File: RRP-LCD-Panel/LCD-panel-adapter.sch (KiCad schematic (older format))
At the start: 4 parts, among them J101 HEADER_18, P101 CONN_4X2, P102 CONN_5X2, P103 CONN_5X2

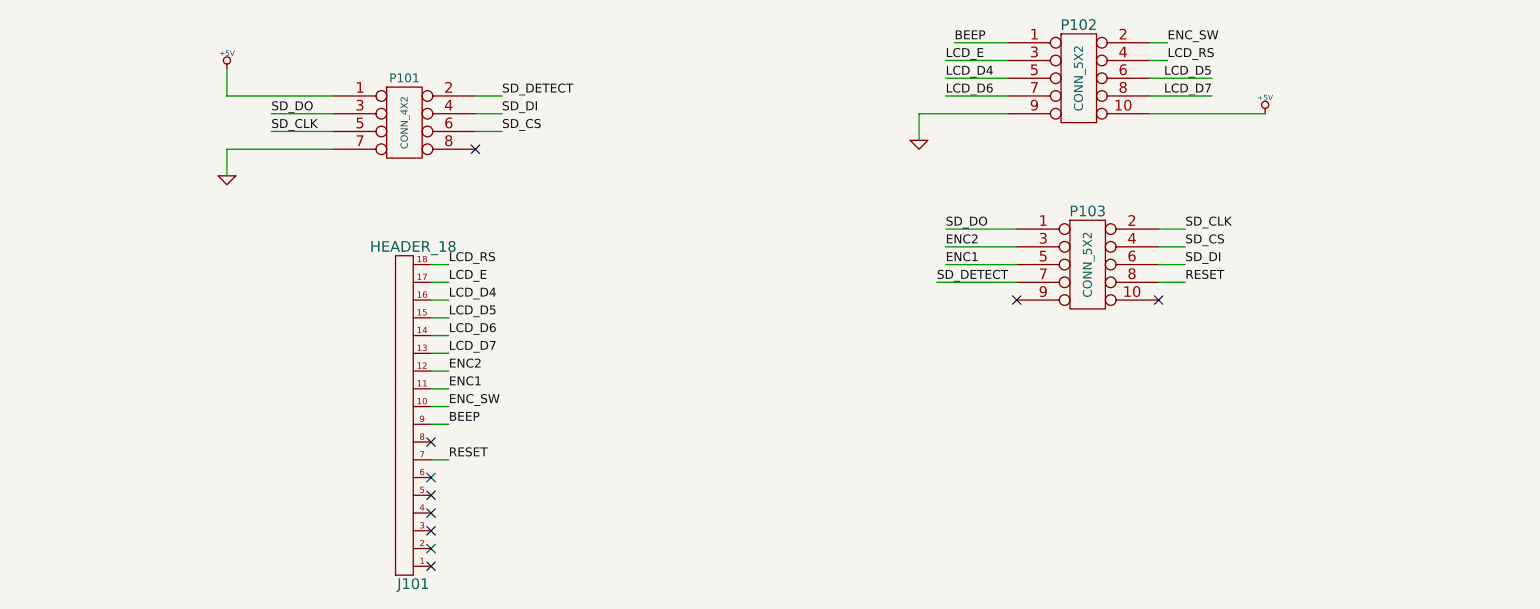
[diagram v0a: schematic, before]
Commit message: RRP-LCD-Panel: update schematics, add PDFS
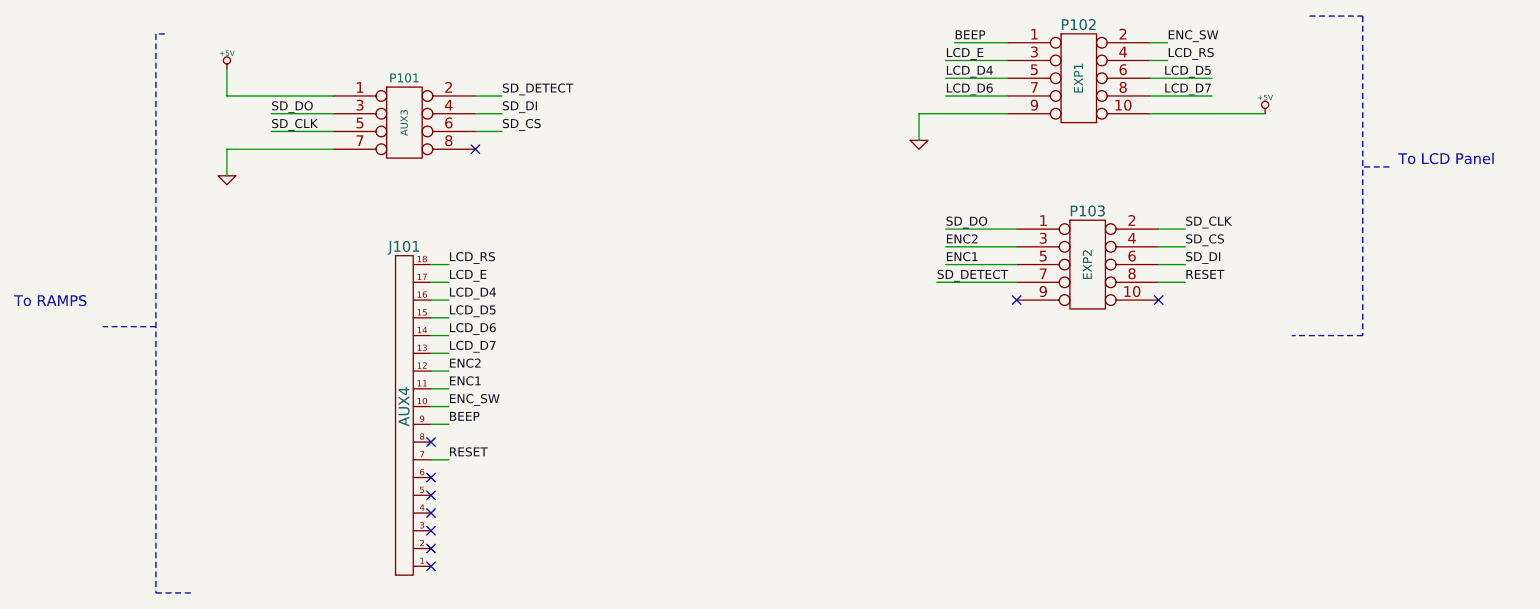
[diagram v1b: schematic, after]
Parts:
- J101: value HEADER_18 -> AUX4
- P101: value CONN_4X2 -> AUX3
- P102: value CONN_5X2 -> EXP1
- P103: value CONN_5X2 -> EXP2
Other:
- note added: "To LCD Panel"
- note added: "To RAMPS"
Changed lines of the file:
@@
 encoding utf-8
 Sheet 1 1
-Title ""
-Date "25 sep 2013"
+Title "RepRap LCD Controller - RAMPS Adapter"
+Date "3 oct 2013"
 Rev ""
-Comp ""
-Comment1 ""
-Comment2 ""
+Comp "Based on http://reprap.org/wiki/RepRapDiscount_Smart_Controller"
+Comment1 "License: GPL"
+Comment2 "Drawn by: Bob Cousins"
 Comment3 ""
 Comment4 ""
@@
 P 6750 1950
 F 0 "P102" H 6750 2250 60  0000 C CNN
-F 1 "CONN_5X2" V 6750 1950 50  0000 C CNN
+F 1 "EXP1" V 6750 1950 50  0000 C CNN
 F 2 "" H 6750 1950 60  0000 C CNN
 F 3 "" H 6750 1950 60  0000 C CNN
@@
 P 6800 3000
 F 0 "P103" H 6800 3300 60  0000 C CNN
-F 1 "CONN_5X2" V 6800 3000 50  0000 C CNN
+F 1 "EXP2" V 6800 3000 50  0000 C CNN
 F 2 "" H 6800 3000 60  0000 C CNN
 F 3 "" H 6800 3000 60  0000 C CNN
@@
 NoConn ~ 7200 3200
 NoConn ~ 6400 3200
-Wire Wire Line
-	7800 2150 7150 2150
-Wire Wire Line
-	7500 2050 7150 2050
-Wire Wire Line
-	6350 2050 6000 2050
-Wire Wire Line
-	7500 1950 7150 1950
-Wire Wire Line
-	6350 1950 6000 1950
-Wire Wire Line
-	6350 2150 5850 2150
-Wire Wire Line
-	5850 2150 5850 2300
-Wire Wire Line
-	6350 1750 6050 1750
-Wire Wire Line
-	6000 1850 6350 1850
-Wire Wire Line
-	7250 1850 7150 1850
-Wire Wire Line
-	7150 1750 7250 1750
-Wire Wire Line
-	5950 3100 6400 3100
-Wire Wire Line
-	6400 3000 6000 3000
-Wire Wire Line
-	6000 2900 6400 2900
-Wire Wire Line
-	6400 2800 6000 2800
-Wire Wire Line
-	7200 2800 7350 2800
-Wire Wire Line
-	7200 2900 7350 2900
-Wire Wire Line
-	7200 3000 7350 3000
-Wire Wire Line
-	7350 3100 7200 3100
 $Comp
 L CONN_4X2 P101
@@
 P 2950 2200
 F 0 "P101" H 2950 2450 50  0000 C CNN
-F 1 "CONN_4X2" V 2950 2200 40  0000 C CNN
+F 1 "AUX3" V 2950 2200 40  0000 C CNN
 F 2 "" H 2950 2200 60  0000 C CNN
 F 3 "" H 2950 2200 60  0000 C CNN
@@
 U 1 1 5243403B
 P 3000 3850
-F 0 "J101" H 3000 4800 60  0000 C CNN
-F 1 "HEADER_18" H 3000 2900 60  0000 C CNN
+F 0 "J101" H 3050 2900 60  0000 C CNN
+F 1 "AUX4" V 3050 3800 60  0000 C CNN
 F 2 "" H 3000 3850 60  0000 C CNN
 F 3 "" H 3000 3850 60  0000 C CNN
@@
 	-1   0    0    -1
 $EndComp
-Wire Wire Line
-	2550 2350 1950 2350
 Text Label 2200 2250 0    50   ~ 0
 SD_CLK
@@
 $EndComp
 NoConn ~ 3350 2350
-Wire Wire Line
-	1950 2050 2550 2050
 Text Label 3500 2250 0    50   ~ 0
 SD_CS
@@
 Text Label 3500 2050 0    50   ~ 0
 SD_DETECT
-Wire Wire Line
-	2550 2250 2200 2250
-Wire Wire Line
-	2200 2150 2550 2150
-Wire Wire Line
-	3350 2250 3500 2250
-Wire Wire Line
-	3500 2150 3350 2150
-Wire Wire Line
-	3350 2050 3500 2050
 NoConn ~ 3100 4700
 NoConn ~ 3100 4600
@@
 Text Label 3200 3000 0    50   ~ 0
 LCD_RS
+Text Notes 8550 2450 0    60   ~ 0
+To LCD Panel
+Wire Wire Line
+	7800 2150 7150 2150
+Wire Wire Line
+	7500 2050 7150 2050
+Wire Wire Line
+	6350 2050 6000 2050
+Wire Wire Line
+	7500 1950 7150 1950
+Wire Wire Line
+	6350 1950 6000 1950
+Wire Wire Line
+	6350 2150 5850 2150
+Wire Wire Line
+	5850 2150 5850 2300
+Wire Wire Line
+	6350 1750 6050 1750
+Wire Wire Line
+	6000 1850 6350 1850
+Wire Wire Line
+	7250 1850 7150 1850
+Wire Wire Line
+	7150 1750 7250 1750
+Wire Wire Line
+	5950 3100 6400 3100
+Wire Wire Line
+	6400 3000 6000 3000
+Wire Wire Line
+	6000 2900 6400 2900
+Wire Wire Line
+	6400 2800 6000 2800
+Wire Wire Line
+	7200 2800 7350 2800
+Wire Wire Line
+	7200 2900 7350 2900
+Wire Wire Line
+	7200 3000 7350 3000
+Wire Wire Line
+	7350 3100 7200 3100
+Wire Wire Line
+	2550 2350 1950 2350
+Wire Wire Line
+	1950 2050 2550 2050
+Wire Wire Line
+	2550 2250 2200 2250
+Wire Wire Line
+	2200 2150 2550 2150
+Wire Wire Line
+	3350 2250 3500 2250
+Wire Wire Line
+	3500 2150 3350 2150
+Wire Wire Line
+	3350 2050 3500 2050
 Wire Wire Line
 	3200 3300 3100 3300
@@
 Wire Wire Line
 	1950 2350 1950 2500
+Wire Notes Line
+	8050 1600 8350 1600
+Wire Notes Line
+	8350 1600 8350 3400
+Wire Notes Line
+	8350 3400 7950 3400
+Wire Notes Line
+	8500 2450 8350 2450
+Wire Notes Line
+	1600 1700 1550 1700
+Wire Notes Line
+	1550 1700 1550 4850
+Wire Notes Line
+	1550 4850 1750 4850
+Wire Notes Line
+	1550 3350 1250 3350
+Text Notes 750  3250 0    60   ~ 0
+To RAMPS
 $EndSCHEMATC
